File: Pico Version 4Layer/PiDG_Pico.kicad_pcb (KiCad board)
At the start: 4 copper layers, 126 x 126 mm, 71 parts, among them J1 Conn_02x05_Odd_Even, J10 Trig, J11 Laser Enable, J12 Pixel Reset, J14 Pico Socket A, J15 Pico Socket B, J16 Laser En/PWM Trig/GND, J17 USB-C PD in, J2 Conn_02x05_Odd_Even, J3 Conn_02x05_Odd_Even, J4 Conn_02x05_Odd_Even, J5 Conn_02x05_Odd_Even, J6 Conn_02x05_Odd_Even, J7 Laser 1, J8 Laser 2, U1 74LVC1G04, U10 74AHCT1G08, U12 74LVC1G17, U13 UCC27524, U14 CH224K, U15 AP63205WU, U16 LM66100, U17 LP2951D, U2 SN74LVC04AD, U3 74LVC1G04, U4 SN74LVC04AD, U5 74LVC1G04, U6 SN74LVC04AD, U7 74AHCT1G08, U8 74AHCT1G08, U9 NCP718xSN180

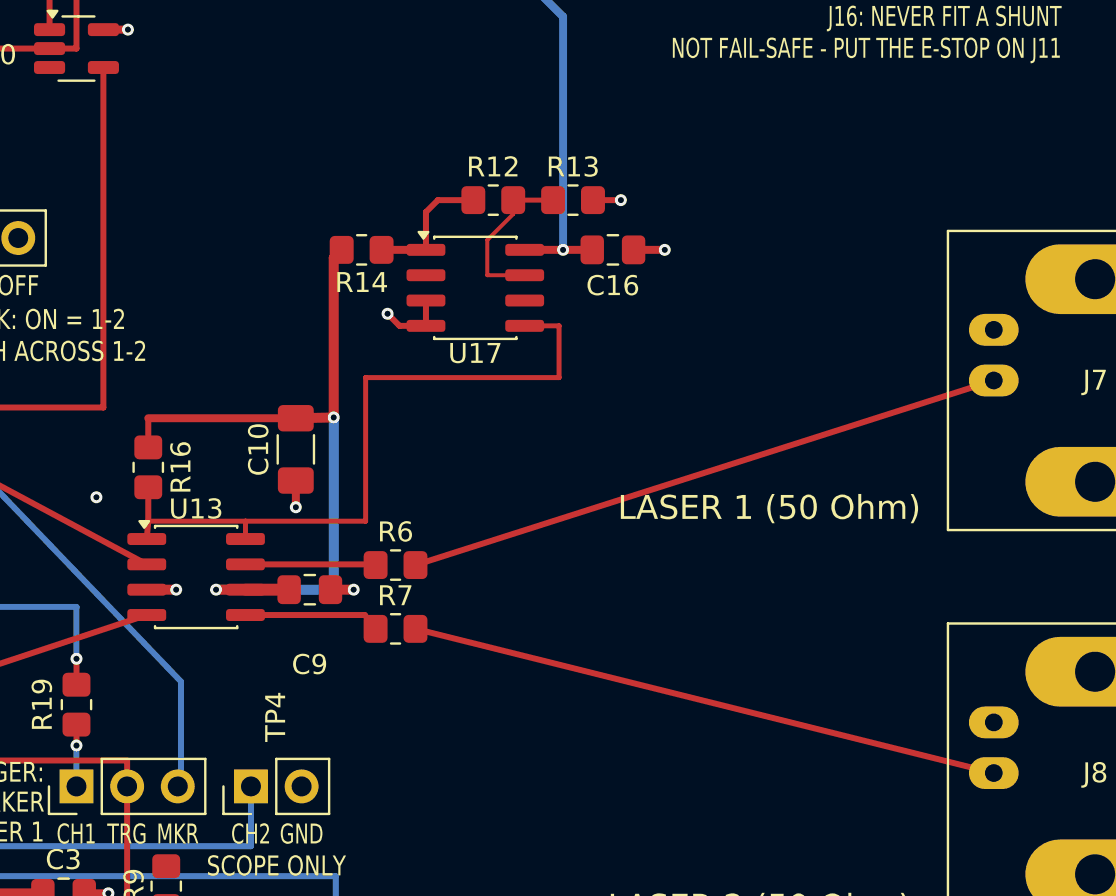
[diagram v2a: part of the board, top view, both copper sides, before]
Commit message: 12 V rail and laser output resistors upgraded: no board duty limit
The laser outputs were limited by the board itself: R6/R7 were 0.125 W 0805
(<= ~19 % duty into 50 ohm) and the LP2951 12 V regulator was rated 100 mA
(both outputs high need ~200 mA). Now the board carries any duty the
firmware accepts, even into a shorted BNC.

- U17 LP2951 SOIC-8 -> LT3065EDD (adjustable, 45 V / 500 mA, DFN-10):
  R12/R13 101k/5.36k 0.1 % -> 11.9 V (11.65-12.17 V worst case), R20 750R
  sets a 400 mA current limit, C18 22 nF on IMAX, C19 10 nF on BYP, C17
  10 uF output cap. R14 (the LP2951's ESR resistor) removed.
- New U18 TPS3700 window comparator (R21/R22/R23 1M/6.04k/31.6k, C20)
  drives LASER_PWR_OK: U13 stays disabled unless +12V is inside
  11.0-13.1 V, which also catches a failed-short regulator.
- R6/R7 69.8R 0805 -> 68R 1 % 2 W 2512. Amplitude into 50 ohm
  4.61-5.08 V (typ 4.84 V), inside the LDP-V's 4.5-5.2 V window.
- Board: U17 cluster rebuilt around (219, 76.5), U18 cluster in the free
  pocket left of the +12V trunk, VBUS_PD fed on B.Cu, R6/R7 re-placed.
  DRC 0 / 0 unconnected, ERC 0, schematic parity equal to the baseline.
- Gerbers, drill, zip, CPL and BOMs (human + JLC, 40 lines / 75 parts,
  all in stock except the already-flagged U9/U14) regenerated;
  README, Hardware.md and JLC_ORDER.md updated.

Co-Authored-By: Claude Opus 5.5 (1M context) <noreply@anthropic.com>
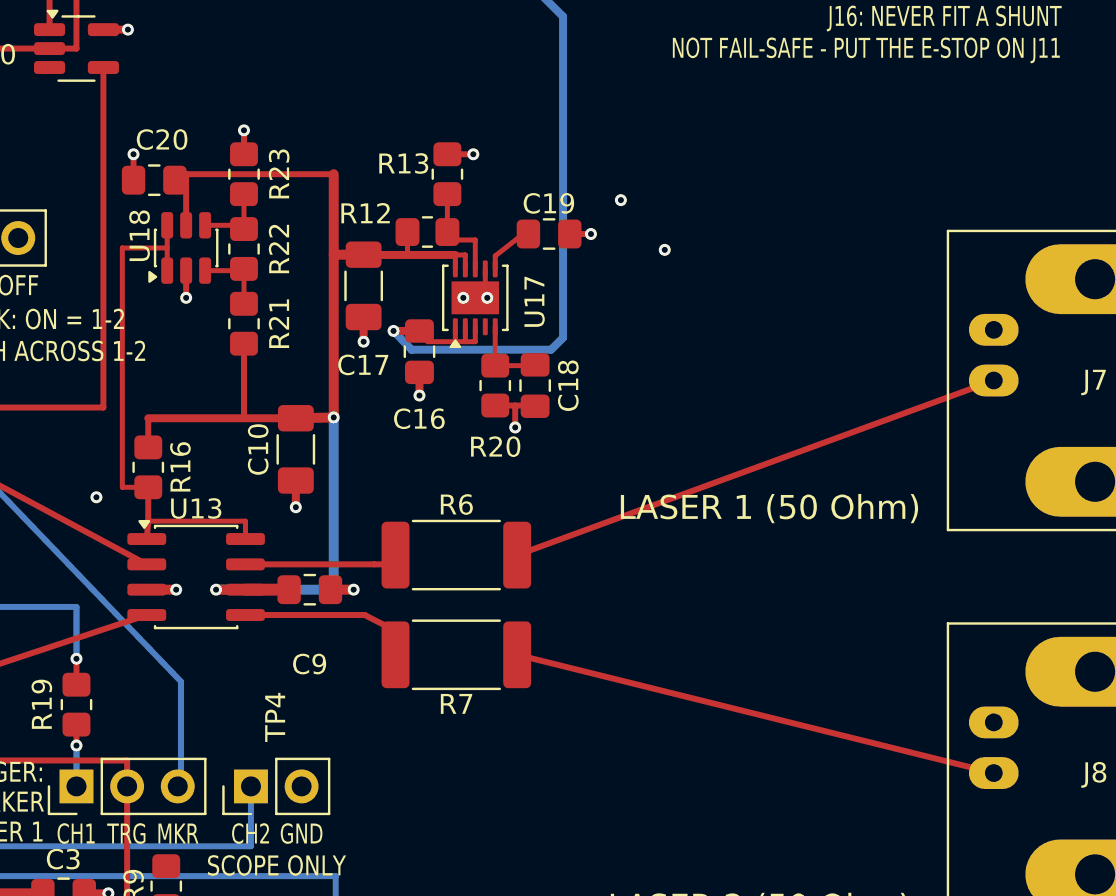
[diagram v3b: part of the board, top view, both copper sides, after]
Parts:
- removed R14: 1R, Resistor_SMD:R_0805_2012Metric_Pad1.20x1.40mm_HandSolder
- added C17: 10uF 50V, Capacitor_SMD:C_1206_3216Metric_Pad1.33x1.80mm_HandSolder, F.Cu at (213.4, 75.9)
- added C18: 22nF, Capacitor_SMD:C_0805_2012Metric_Pad1.18x1.45mm_HandSolder, F.Cu at (222.0, 80.9)
- added C19: 10nF, Capacitor_SMD:C_0805_2012Metric_Pad1.18x1.45mm_HandSolder, F.Cu at (222.7, 73.3)
- added C20: 0.1uF, Capacitor_SMD:C_0805_2012Metric_Pad1.18x1.45mm_HandSolder, F.Cu at (202.9, 70.6)
- added R20: 750, Resistor_SMD:R_0805_2012Metric_Pad1.20x1.40mm_HandSolder, F.Cu at (220.0, 80.9)
- added R21: 1M, Resistor_SMD:R_0805_2012Metric_Pad1.20x1.40mm_HandSolder, F.Cu at (207.4, 77.8)
- added R22: 6.04k, Resistor_SMD:R_0805_2012Metric_Pad1.20x1.40mm_HandSolder, F.Cu at (207.4, 74.0)
- added R23: 31.6k, Resistor_SMD:R_0805_2012Metric_Pad1.20x1.40mm_HandSolder, F.Cu at (207.4, 70.3)
- added U18: TPS3700DDC, Package_TO_SOT_SMD:SOT-23-6, F.Cu at (204.5, 74.0)
- R12: value 100k -> 101k
- R13: value 11.3k -> 5.36k
- R6, R7: value 69.8 -> 68; footprint Resistor_SMD:R_0805_2012Metric_Pad1.20x1.40mm_HandSolder -> Resistor_SMD:R_2512_6332Metric_Pad1.40x3.35mm_HandSolder
- U17: value LP2951D -> LT3065EDD; footprint Package_SO:SOIC-8_3.9x4.9mm_P1.27mm -> Package_DFN_QFN:DFN-10-1EP_3x3mm_P0.5mm_EP1.65x2.38mm
- moved C16 11.0 mm to (216.2, 79.2), turned to -90 degrees
- moved R13 6.43 mm to (217.6, 70.3), turned to 90 degrees
- moved R12 3.67 mm to (216.6, 73.2)
- moved R7 3.32 mm to (218.1, 94.4)
- moved R6 3.09 mm to (218.1, 89.4)
- moved U17 0.50 mm to (219.0, 76.5), turned to 90 degrees
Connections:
- R12 pad 1: LDO12_OUT -> +12V
- R12 pad 2: FB12 -> Net-(U17-ADJ)
- R13 pad 1: FB12 -> Net-(U17-ADJ)
- U17 pad 1: LDO12_OUT -> VBUS_PD
- U17 pad 2: unconnected-(U17-SENSE-Pad2) -> VBUS_PD
- U17 pad 3: GND -> VBUS_PD
- U17 pad 4: GND -> unconnected-(U17-PWRGD-Pad4)
- U17 pad 5: LASER_PWR_OK -> Net-(U17-IMAX)
- U17 pad 6: unconnected-(U17-VTAP-Pad6) -> Net-(U17-BYP)
- U17 pad 7: FB12 -> GND
- U17 pad 8: VBUS_PD -> Net-(U17-ADJ)
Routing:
- net +12V: track 37.5 -> 64.0 mm
- net VBUS_PD: track 78.9 -> 95.1 mm
- net LASER_PWR_OK: track 35.6 -> 26.2 mm
- net FB12: track 8.18 -> 0.00 mm
- net LDO12_OUT: track 6.74 -> 0.00 mm
- net GND: track 51.7 -> 57.9 mm, vias 84 -> 93
- net CH2_DRIVE: track 29.9 -> 24.6 mm
- net CH1_DRIVE: track 30.4 -> 25.5 mm
- net Net-(U17-ADJ): track 0.00 -> 4.35 mm
- net Net-(U17-IMAX): track 0.00 -> 3.95 mm
- net Net-(U18-INB-): track 0.00 -> 3.70 mm
- net Net-(U18-INA+): track 0.00 -> 3.70 mm
- net Net-(U17-BYP): track 0.00 -> 2.43 mm
- net CH1_DRIVE_RAW: track 6.53 -> 7.53 mm
- net CH2_DRIVE_RAW: track 6.86 -> 7.72 mm

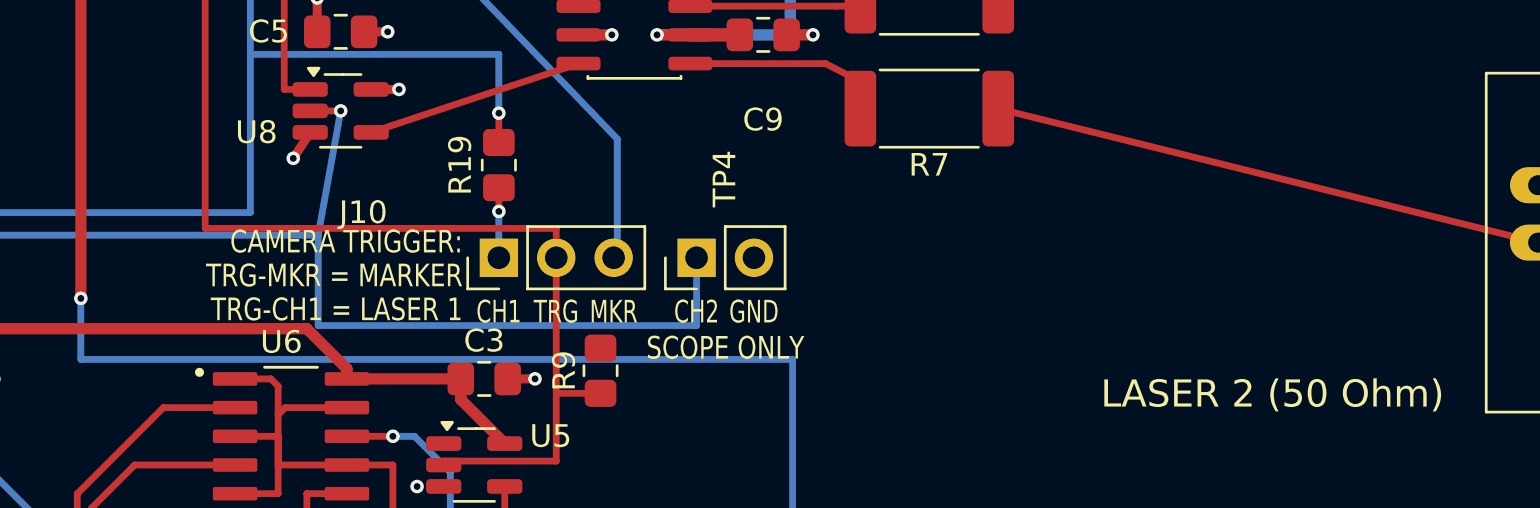
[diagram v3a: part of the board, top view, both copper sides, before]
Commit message: Move J10 into the open block east of TP4; TP4 2.54 mm west
J10 (camera trigger select) was wedged between U13, U5/R9, its three-line
key and TP4, whose labels ran into it so "CH1 TRG MKR CH2 GND" read like
one 5-pin header. J10 now sits on its own at x 217-222, y 101, in the
previously empty block east of TP4, with the CAMERA TRIGGER key to its
right. TP4 moved 2.54 mm west into the space J10 left, ~9 mm from J10.

- CH1_J10: F.Cu lane from R19 over TP4 (R19 still at the CH1 tap, so
  the laser CH1 timing is unchanged; TRG-CH1 camera trigger ~0.1 ns later).
- PWM_Trig (marker): B.Cu run ends at a new via, F.Cu lane over TP4.
- PWM_TRIG_TAP: ~20 mm branch off the x = 201.54 trunk, under TP4.
- DRC 0 / 0 unconnected, parity unchanged; gerbers, drill, zip and both
  CPLs regenerated (BOMs unchanged); README and Hardware.md updated.

Co-Authored-By: Claude Opus 5.5 (1M context) <noreply@anthropic.com>
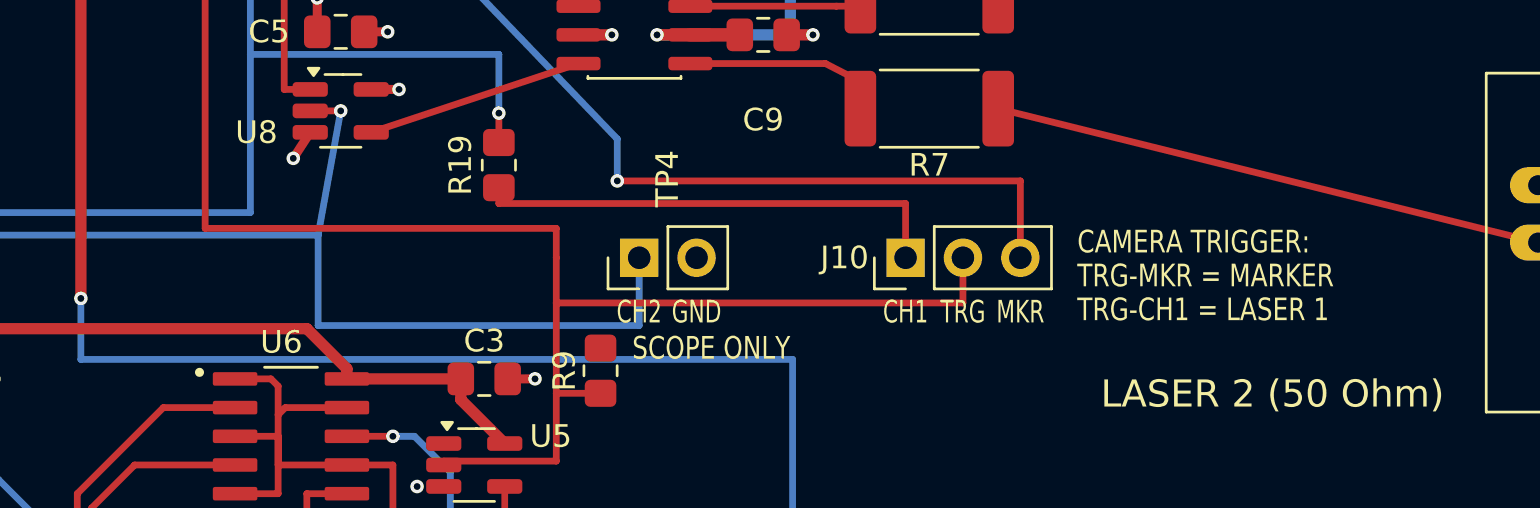
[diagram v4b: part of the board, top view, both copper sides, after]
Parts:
- moved J10 18.0 mm to (217.0, 101.0)
- moved TP4 2.54 mm to (205.2, 101.0)
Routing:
- net PWM_TRIG_TAP: track 152.2 -> 172.2 mm
- net CH1_J10: track 3.10 -> 21.1 mm, vias 1 -> 0
- net PWM_Trig: track 68.8 -> 86.6 mm, vias 0 -> 1
- net _PULSE_OUT_CH2: track 97.9 -> 95.4 mm
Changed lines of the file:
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@@
 	(footprint "Connector_PinHeader_2.54mm:PinHeader_1x02_P2.54mm_Vertical"
 		(layer "F.Cu")
-		(at 207.75 101 90)
+		(at 205.21 101 90)
 		(descr "Through hole straight pin header, 1x02, 2.54mm pitch, single row")
 		(tags "Through hole pin header THT 1x02 2.54mm single row")
@@
 	(footprint "Connector_PinHeader_2.54mm:PinHeader_1x03_P2.54mm_Vertical"
 		(layer "F.Cu")
-		(at 199 101 90)
+		(at 217 101 90)
 		(descr "Through hole straight pin header, 1x03, 2.54mm pitch, single row")
 		(tags "Through hole pin header THT 1x03 2.54mm single row")
 		(property "Reference" "J10"
-			(at 2 -6 0)
+			(at 0 -2.7 0)
 			(layer "F.SilkS")
 			(effects
@@
 		(layer "Edge.Cuts")
 	)
-	(gr_text "CH1"
-		(at 199 103.4 0)
+	(gr_text "CH2"
+		(at 205.21 103.4 0)
 		(layer "F.SilkS")
 		(effects
@@
 		)
 	)
-	(gr_text "TRG"
-		(at 201.54 103.4 0)
+	(gr_text "GND"
+		(at 207.75 103.4 0)
 		(layer "F.SilkS")
 		(effects
@@
 		)
 	)
-	(gr_text "MKR"
-		(at 204.08 103.4 0)
+	(gr_text "CH1"
+		(at 217 103.4 0)
 		(layer "F.SilkS")
 		(effects
@@
 		)
 	)
-	(gr_text "CH2"
-		(at 207.75 103.4 0)
+	(gr_text "TRG"
+		(at 219.54 103.4 0)
 		(layer "F.SilkS")
 		(effects
@@
 		)
 	)
-	(gr_text "GND"
-		(at 210.29 103.4 0)
+	(gr_text "MKR"
+		(at 222.08 103.4 0)
 		(layer "F.SilkS")
 		(effects
@@
 		)
 	)
-	(gr_text "1"
-		(at 156.4 32.384999 0)
+	(gr_text "CAMERA TRIGGER:"
+		(at 224.6 100.3 0)
 		(layer "F.SilkS")
 		(effects
@@
 				(thickness 0.15)
 			)
+			(justify left)
 		)
 	)
-	(gr_text "CONTROL / PROGRAM"
-		(at 168.905 34.2 0)
+	(gr_text "TRG-MKR = MARKER"
+		(at 224.6 101.8 0)
 		(layer "F.SilkS")
 		(effects
@@
 				(thickness 0.15)
 			)
+			(justify left)
 		)
 	)
-	(gr_text "PICO MICRO-USB"
-		(at 168.905 35.8 0)
+	(gr_text "TRG-CH1 = LASER 1"
+		(at 224.6 103.3 0)
 		(layer "F.SilkS")
 		(effects
@@
 				(thickness 0.15)
 			)
+			(justify left)
 		)
 	)
-	(gr_text "ON"
-		(at 191 75.9 0)
+	(gr_text "1"
+		(at 156.4 32.384999 0)
 		(layer "F.SilkS")
 		(effects
@@
 		)
 	)
-	(gr_text "LASER INTERLOCK: ON = 1-2"
-		(at 193.54 77.6 0)
+	(gr_text "CONTROL / PROGRAM"
+		(at 168.905 34.2 0)
 		(layer "F.SilkS")
 		(effects
@@
 		)
 	)
-	(gr_text "E-STOP: NC SWITCH ACROSS 1-2"
-		(at 193.54 79.2 0)
+	(gr_text "PICO MICRO-USB"
+		(at 168.905 35.8 0)
 		(layer "F.SilkS")
 		(effects
@@
 		)
 	)
-	(gr_text "OFF"
-		(at 196.08 75.9 0)
+	(gr_text "ON"
+		(at 191 75.9 0)
 		(layer "F.SilkS")
 		(effects
@@
 		)
 	)
-	(gr_text "SCOPE ONLY"
-		(at 209.02 105 0)
+	(gr_text "LASER INTERLOCK: ON = 1-2"
+		(at 193.54 77.6 0)
 		(layer "F.SilkS")
 		(effects
@@
 		)
 	)
-	(gr_text "CAMERA TRIGGER:"
-		(at 197.4 100.3 0)
+	(gr_text "E-STOP: NC SWITCH ACROSS 1-2"
+		(at 193.54 79.2 0)
 		(layer "F.SilkS")
 		(effects
@@
 				(thickness 0.15)
 			)
-			(justify right)
 		)
 	)
-	(gr_text "TRG-MKR = MARKER"
-		(at 197.4 101.8 0)
+	(gr_text "OFF"
+		(at 196.08 75.9 0)
 		(layer "F.SilkS")
 		(effects
@@
 				(thickness 0.15)
 			)
-			(justify right)
 		)
 	)
-	(gr_text "TRG-CH1 = LASER 1"
-		(at 197.4 103.3 0)
+	(gr_text "SCOPE ONLY"
+		(at 208.4 105 0)
 		(layer "F.SilkS")
 		(effects
@@
 				(thickness 0.15)
 			)
-			(justify right)
 		)
 	)
@@
 	)
 	(segment
+		(start 201.54 103)
+		(end 219.54 103)
+		(width 0.3)
+		(layer "F.Cu")
+		(net "PWM_TRIG_TAP")
+	)
+	(segment
 		(start 252 53)
 		(end 252 57.54)
@@
 	)
 	(segment
+		(start 219.54 103)
+		(end 219.54 101)
+		(width 0.3)
+		(layer "F.Cu")
+		(net "PWM_TRIG_TAP")
+	)
+	(segment
 		(start 186 99.7)
 		(end 186 53)
@@
 	)
 	(segment
-		(start 207.75 104)
+		(start 205.21 104)
 		(end 191 104)
 		(width 0.3)
@@
 	)
 	(segment
-		(start 207.75 101)
-		(end 207.75 104)
+		(start 205.21 101)
+		(end 205.21 104)
 		(width 0.3)
 		(layer "B.Cu")
@@
 	(segment
 		(start 199 97.9)
-		(end 199 98.95)
+		(end 199 98.6)
 		(width 0.3)
 		(layer "F.Cu")
 		(net "CH1_J10")
 	)
-	(via
-		(at 199 98.95)
-		(size 0.6)
-		(drill 0.3)
-		(layers "F.Cu" "B.Cu")
+	(segment
+		(start 199 98.6)
+		(end 217 98.6)
+		(width 0.3)
+		(layer "F.Cu")
 		(net "CH1_J10")
 	)
 	(segment
-		(start 199 98.95)
-		(end 199 101)
+		(start 217 98.6)
+		(end 217 101)
 		(width 0.3)
-		(layer "B.Cu")
+		(layer "F.Cu")
 		(net "CH1_J10")
 	)
@@
 	)
 	(segment
-		(start 163.5 70.278)
-		(end 163.5 83.185)
+		(start 222.08 97.6)
+		(end 222.08 101)
 		(width 0.3)
-		(layer "B.Cu")
+		(layer "F.Cu")
 		(net "PWM_Trig")
 	)
 	(segment
-		(start 161.167 67.945)
-		(end 163.5 70.278)
+		(start 204.24 97.6)
+		(end 222.08 97.6)
+		(width 0.3)
+		(layer "F.Cu")
+		(net "PWM_Trig")
+	)
+	(via
+		(at 204.24 97.6)
+		(size 0.6)
+		(drill 0.3)
+		(layers "F.Cu" "B.Cu")
+		(net "PWM_Trig")
+	)
+	(segment
+		(start 163.5 70.278)
+		(end 163.5 83.185)
 		(width 0.3)
 		(layer "B.Cu")
@@
 	)
 	(segment
-		(start 204.24 100.84)
-		(end 204.08 101)
+		(start 161.167 67.945)
+		(end 163.5 70.278)
 		(width 0.3)
 		(layer "B.Cu")
@@
 	(segment
 		(start 204.24 95.742)
-		(end 204.24 100.84)
+		(end 204.24 97.6)
 		(width 0.3)
 		(layer "B.Cu")
